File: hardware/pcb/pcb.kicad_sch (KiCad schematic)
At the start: 5 parts, among them SW1 RotaryEncoder_Switch, U1 AMS1117-3.3, U2 MCP23017_SP, U3 ESP32-S3, U4 MT3608

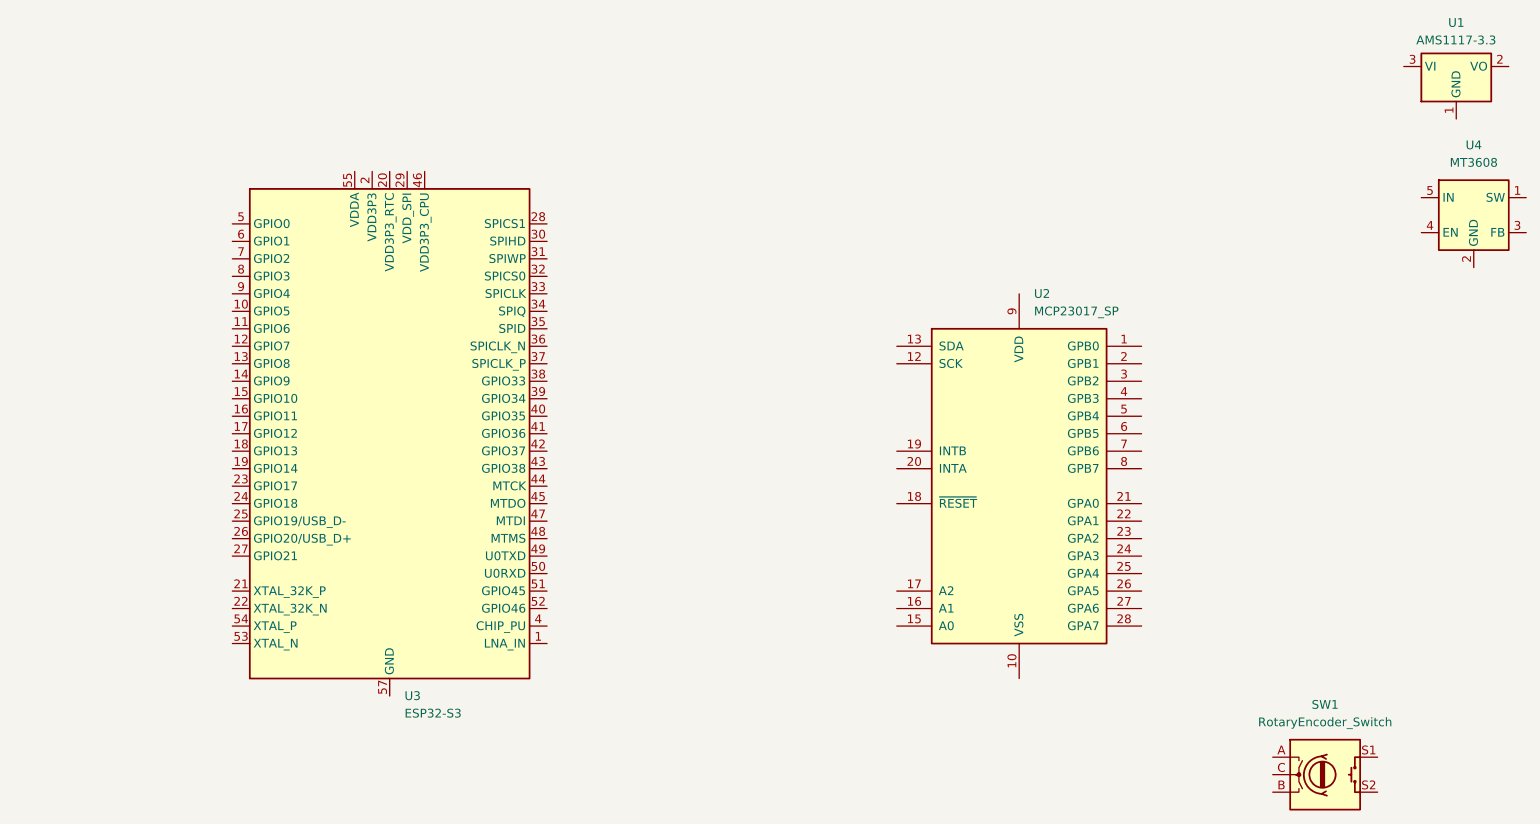
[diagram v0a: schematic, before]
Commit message: KiCad PowerSupply
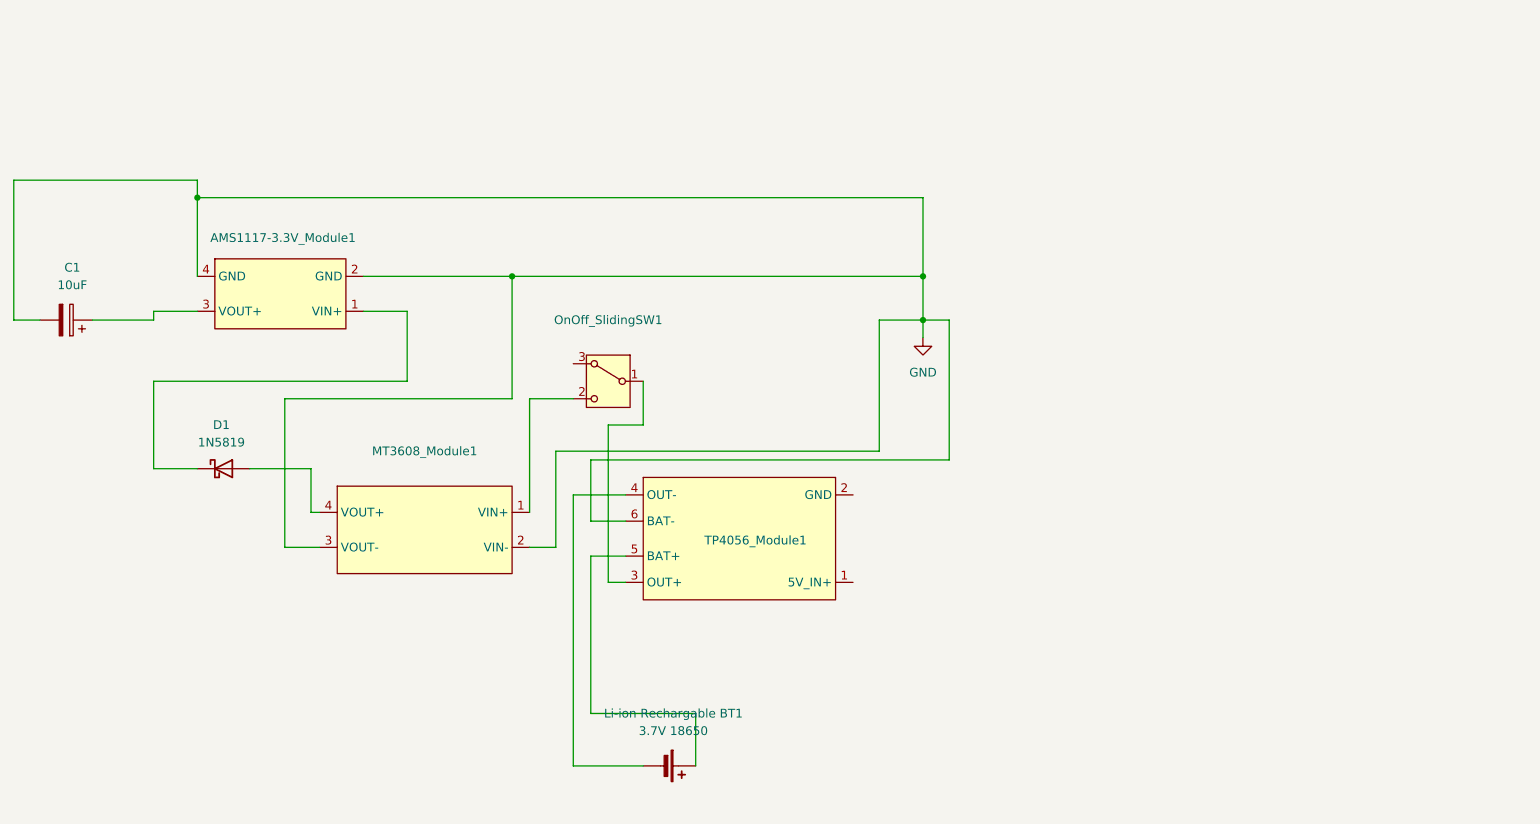
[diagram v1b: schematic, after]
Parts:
- removed SW1: RotaryEncoder_Switch, symbol Device:RotaryEncoder_Switch
- removed U1: AMS1117-3.3, Package_TO_SOT_SMD:SOT-223-3_TabPin2, symbol Regulator_Linear:AMS1117-3.3
- removed U2: MCP23017_SP, Package_DIP:DIP-28_W7.62mm, symbol Interface_Expansion:MCP23017_SP
- removed U3: ESP32-S3, RF_Module:ESP32-S3-WROOM-1, symbol MCU_Espressif:ESP32-S3
- removed U4: MT3608, Package_TO_SOT_SMD:SOT-23-6_Handsoldering, symbol Regulator_Switching:MT3608
- added AMS1117-3.3V_Module1: ~, TMB_Library:AMS1117-3.3V, symbol TMB_Library:AMS1117-3.3V_Module
- added C1: 10uF, Capacitor_THT:CP_Axial_L11.0mm_D5.0mm_P18.00mm_Horizontal, symbol Device:C_Polarized
- added D1: 1N5819, Diode_THT:D_DO-41_SOD81_P10.16mm_Horizontal, symbol Diode:1N5819
- added Li-ion Rechargable BT1: 3.7V 18650, Battery:BatteryHolder_MPD_BK-18650-PC2, symbol Device:Battery_Cell
- added MT3608_Module1: ~, TMB_Library:MT3608-hw-045, symbol TMB_Library:MT3608_Module
- added OnOff_SlidingSW1: SW_Wuerth_450301014042, Button_Switch_THT:SW_Slide-03_Wuerth-WS-SLTV_10x2.5x6.4_P2.54mm, symbol Switch:SW_Wuerth_450301014042
- added TP4056_Module1: ~, TMB_Library:TP4056-18650, symbol TMB_Library:TP4056_Module
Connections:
- new net: MT3608_Module1.1 (VIN+), OnOff_SlidingSW1.2 (C)
- new net: D1.2 (A), MT3608_Module1.4 (VOUT+)
- new net: AMS1117-3.3V_Module1.3 (VOUT+), C1.1
- new net: OnOff_SlidingSW1.1 (B), TP4056_Module1.3 (OUT+)
- new net: Li-ion Rechargable BT1.2 (-), TP4056_Module1.4 (OUT-)
- new net: Li-ion Rechargable BT1.1 (+), TP4056_Module1.5 (BAT+)
- new net: AMS1117-3.3V_Module1.1 (VIN+), D1.1 (K)
- new net GND: AMS1117-3.3V_Module1.2 (GND), AMS1117-3.3V_Module1.4 (GND), C1.2, MT3608_Module1.2 (VIN-), MT3608_Module1.3 (VOUT-), TP4056_Module1.6 (BAT-)
